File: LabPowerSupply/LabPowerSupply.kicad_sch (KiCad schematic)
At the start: 82 parts, among them SW00 7, SW01 8, SW02 7, SW03 Voltage 1, SW04 Channel 1, SW10 4, SW11 5, SW12 6, SW13 Current 1, SW14 Channel 2, SW20 1, SW21 2, SW22 3, SW23 Voltage 2, SW24 Confirm, SW30 Decimal, SW31 0, SW32 Backspace, SW33 Current 2, SW34 Cancel

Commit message: tmp
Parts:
- R1_ADC, R2_ADC: footprint (none) -> Resistor_SMD:R_1210_3225Metric
- gave numbers to parts that had none: 1
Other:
- added sheet TransformerBR (TransformerBR.kicad_sch)
- moved on the sheet: C1_Charge, C2_Charge, D1_Charge, D2_Charge, Q_Charge, R41, R42, R43, R44, R45, R46, R47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

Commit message: Fixing my screwup
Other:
- removed sheet TransformerBR
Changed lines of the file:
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@@
     )
-  )
-  (hierarchical_label "AC Power" (shape input) (at 16.51 34.29 0)
-    (effects (font (size 1.27 1.27)) (justify left))
   )
   (symbol (lib_id "power:+3V3") (at 116.84 54.61 0) (unit 1)
@@
     (pin "1")
   )
-  (sheet (at 12.7 12.7) (size 96.52 45.72) (fields_autoplaced)
-    (stroke (width 0.1524) (type solid) (color 0 0 0 0))
-    (fill (color 0 0 0 0.0000))
-    (property "Sheet name" "TransformerBR" (id 0) (at 12.7 11.9884 0)
-      (effects (font (size 1.27 1.27)) (justify left bottom))
-    )
-    (property "Sheet file" "TransformerBR.kicad_sch" (id 1) (at 12.7 59.0046 0)
-      (effects (font (size 1.27 1.27)) (justify left top))
-    )
-  )
   (sheet_instances
     (path "/" (page "1"))
-    (path "/a7d0e103-1391-4f13-b0bc-d947ebd08577" (page "2"))
   )
   (symbol_instances

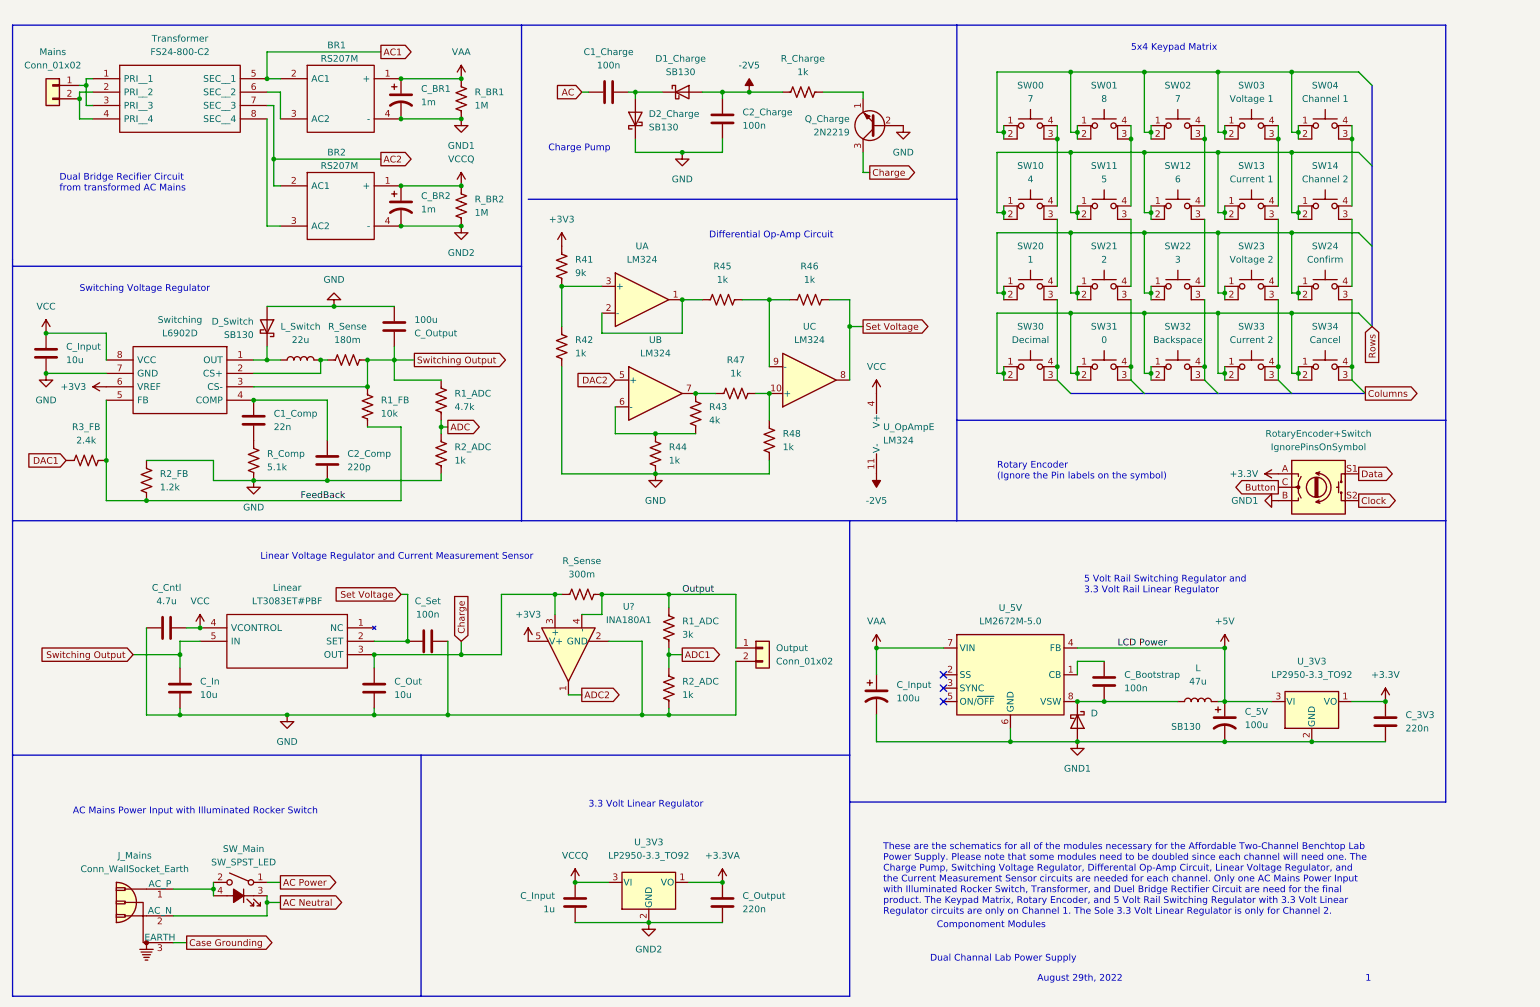
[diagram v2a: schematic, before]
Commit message: basic hierarchiral schematics
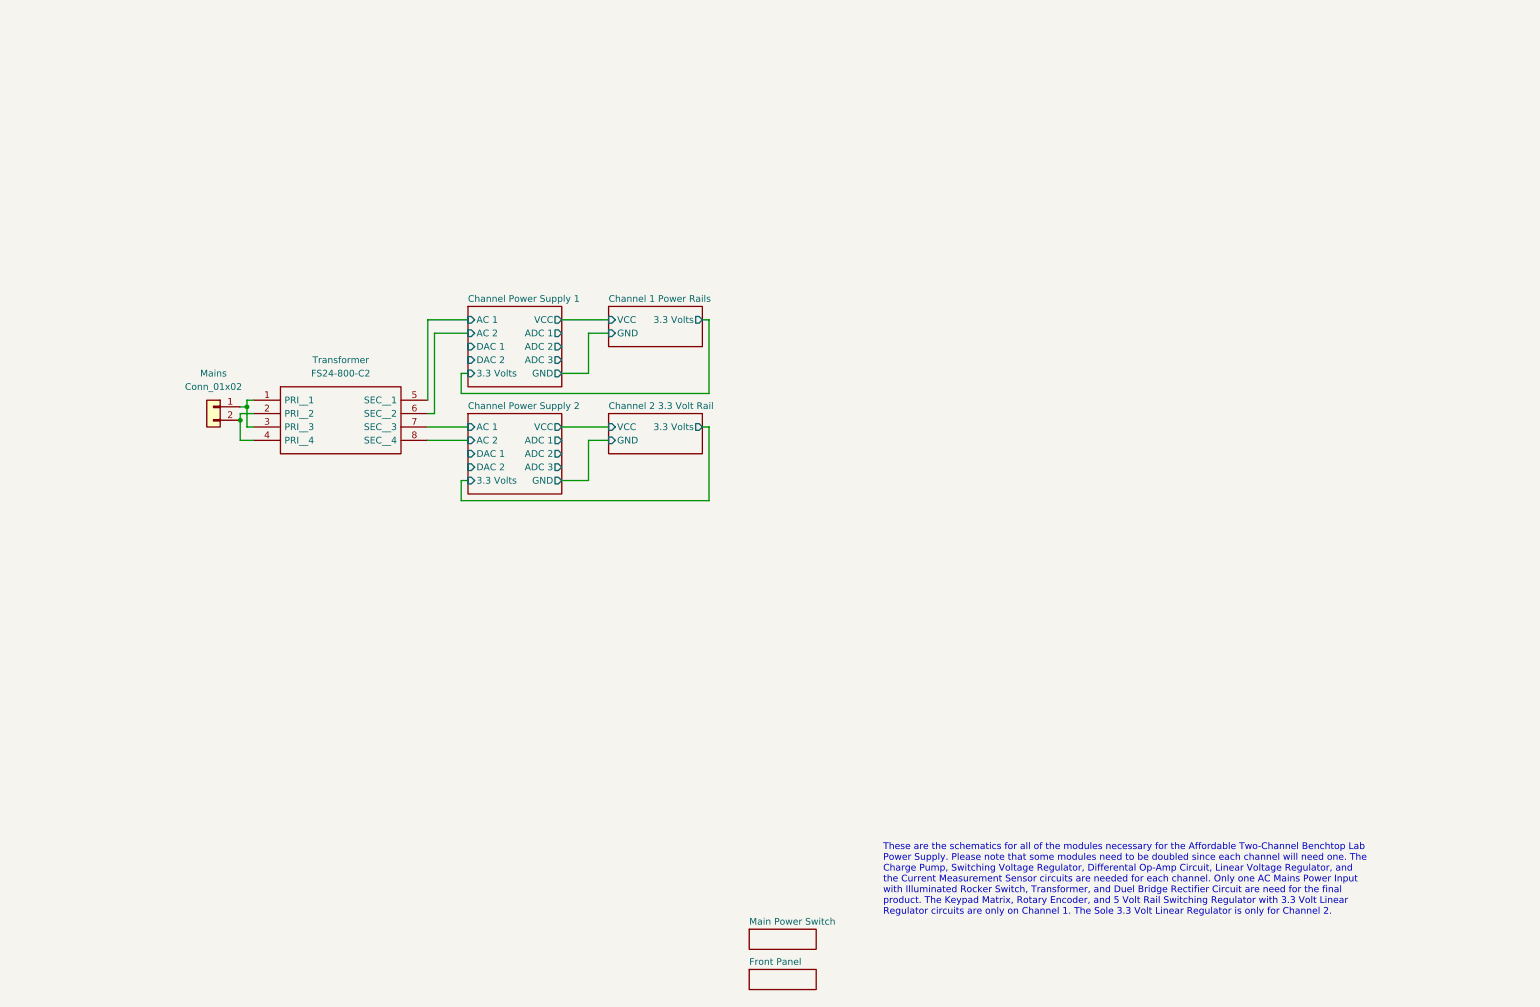
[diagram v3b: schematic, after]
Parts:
- removed BR1, BR2: RS207M, SamacSys_Parts:RS207M, symbol SamacSys_Parts:RS207M
- removed C1_Charge, C2_Charge, C_Bootstrap, C_Set: 100n, Capacitor_SMD:C_1210_3225Metric, symbol Device:C
- removed C1_Comp: 22n, Capacitor_SMD:C_1210_3225Metric, symbol Device:C
- removed C2_Comp: 220p, Capacitor_SMD:C_1210_3225Metric, symbol Device:C
- removed C_3V3, C_Output: 220n, Capacitor_SMD:C_1210_3225Metric, symbol Device:C
- removed C_5V, C_Input: 100u, Capacitor_THT:CP_Radial_D12.5mm_P5.00mm, symbol Device:C_Polarized_US
- removed C_BR1, C_BR2: 1m, Capacitor_THT:C_Radial_D12.5mm_H25.0mm_P5.00mm, symbol Device:C_Polarized_US
- removed C_Cntl: 4.7u, Capacitor_SMD:C_1210_3225Metric, symbol Device:C
- removed C_In, C_Out: 10u, Capacitor_SMD:C_1210_3225Metric, symbol Device:C
- removed C_Input: 10u, symbol Device:C
- removed C_Input: 1u, Capacitor_SMD:C_1210_3225Metric, symbol Device:C
- removed C_Output: 100u, Capacitor_SMD:C_1210_3225Metric, symbol Device:C
- removed D, D1_Charge, D2_Charge, D_Switch: SB130, Diode_THT:D_DO-41_SOD81_P10.16mm_Horizontal, symbol Diode:SB130
- removed J_Mains: Conn_WallSocket_Earth, symbol Connector:Conn_WallSocket_Earth
- removed L: 47u, Inductor_SMD:L_1210_3225Metric, symbol Device:L
- removed L_Switch: 22u, Inductor_SMD:L_1210_3225Metric, symbol Device:L
- removed Linear: LT3083ET#PBF, TO170P457X1022X2306-5P, symbol SamacSys_Parts:LT3083ET#PBF
- removed Output: Conn_01x02, Connector_Wire:SolderWire-2sqmm_1x02_P7.8mm_D2mm_OD3.9mm, symbol Connector_Generic:Conn_01x02
- removed Q_Charge: 2N2219, Package_TO_SOT_THT:TO-39-3, symbol Transistor_BJT:2N2219
- removed R1_ADC: 4.7k, Resistor_SMD:R_1210_3225Metric, symbol Device:R_US
- removed R1_ADC: 3k, Resistor_SMD:R_1210_3225Metric, symbol Device:R_US
- removed R1_FB: 10k, Resistor_SMD:R_1210_3225Metric, symbol Device:R_US
- removed R2_ADC (x2), R42, R44, R45, R46, R47, R48: 1k, Resistor_SMD:R_1210_3225Metric, symbol Device:R_US
- removed R2_FB: 1.2k, Resistor_SMD:R_1210_3225Metric, symbol Device:R_US
- removed R3_FB: 2.4k, Resistor_SMD:R_1210_3225Metric, symbol Device:R_US
- removed R41: 9k, Resistor_SMD:R_1210_3225Metric, symbol Device:R_US
- removed R43: 4k, Resistor_SMD:R_1210_3225Metric, symbol Device:R_US
- removed R_BR1, R_BR2: 1M, Resistor_SMD:R_1210_3225Metric, symbol Device:R_US
- removed R_Charge: 1k, symbol Device:R_US
- removed R_Comp: 5.1k, Resistor_SMD:R_1210_3225Metric, symbol Device:R_US
- removed R_Sense: 180m, Resistor_SMD:R_1210_3225Metric, symbol Device:R_US
- removed R_Sense: 300m, Resistor_SMD:R_1210_3225Metric, symbol Device:R_US
- removed RotaryEncoder+Switch: IgnorePinsOnSymbol, symbol Device:RotaryEncoder_Switch
- removed SW00, SW02: 7, Button_Switch_SMD:SW_MEC_5GSH9, symbol Switch:SW_MEC_5E
- removed SW01: 8, Button_Switch_SMD:SW_MEC_5GSH9, symbol Switch:SW_MEC_5E
- removed SW03: Voltage 1, Button_Switch_SMD:SW_MEC_5GSH9, symbol Switch:SW_MEC_5E
- removed SW04: Channel 1, Button_Switch_SMD:SW_MEC_5GSH9, symbol Switch:SW_MEC_5E
- removed SW10: 4, Button_Switch_SMD:SW_MEC_5GSH9, symbol Switch:SW_MEC_5E
- removed SW11: 5, Button_Switch_SMD:SW_MEC_5GSH9, symbol Switch:SW_MEC_5E
- removed SW12: 6, Button_Switch_SMD:SW_MEC_5GSH9, symbol Switch:SW_MEC_5E
- removed SW13: Current 1, Button_Switch_SMD:SW_MEC_5GSH9, symbol Switch:SW_MEC_5E
- removed SW14: Channel 2, Button_Switch_SMD:SW_MEC_5GSH9, symbol Switch:SW_MEC_5E
- removed SW20: 1, Button_Switch_SMD:SW_MEC_5GSH9, symbol Switch:SW_MEC_5E
- removed SW21: 2, Button_Switch_SMD:SW_MEC_5GSH9, symbol Switch:SW_MEC_5E
- removed SW22: 3, Button_Switch_SMD:SW_MEC_5GSH9, symbol Switch:SW_MEC_5E
- removed SW23: Voltage 2, Button_Switch_SMD:SW_MEC_5GSH9, symbol Switch:SW_MEC_5E
- removed SW24: Confirm, Button_Switch_SMD:SW_MEC_5GSH9, symbol Switch:SW_MEC_5E
- removed SW30: Decimal, Button_Switch_SMD:SW_MEC_5GSH9, symbol Switch:SW_MEC_5E
- removed SW31: 0, Button_Switch_SMD:SW_MEC_5GSH9, symbol Switch:SW_MEC_5E
- removed SW32: Backspace, Button_Switch_SMD:SW_MEC_5GSH9, symbol Switch:SW_MEC_5E
- removed SW33: Current 2, Button_Switch_SMD:SW_MEC_5GSH9, symbol Switch:SW_MEC_5E
- removed SW34: Cancel, Button_Switch_SMD:SW_MEC_5GSH9, symbol Switch:SW_MEC_5E
- removed SW_Main: SW_SPST_LED, symbol Switch:SW_SPST_LED
- removed Switching: L6902D, SOIC127P600X175-8N, symbol SamacSys_Parts:L6902D
- removed U, U_OpAmp: LM324, Package_SO:SOIC-14_3.9x8.7mm_P1.27mm, symbol Amplifier_Operational:LM324
- removed U?: INA180A1, Package_TO_SOT_SMD:SOT-23-5, symbol Amplifier_Current:INA180A1
- removed U_3V3 (x2): LP2950-3.3_TO92, Package_TO_SOT_THT:TO-92_Inline, symbol Regulator_Linear:LP2950-3.3_TO92
- removed U_5V: LM2672M-5.0, Package_SO:SOIC-8_3.9x4.9mm_P1.27mm, symbol Regulator_Switching:LM2672M-5.0
- Mains: footprint Connector_Wire:SolderWire-2sqmm_1x02_P7.8mm_D2mm_OD3.9mm -> Connector_TE-Connectivity:TE_MATE-N-LOK_1-770866-x_1x02_P4.14mm_Vertical
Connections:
- net Channel Power Supply 2/AC 2: now reaches Transformer.8 (SEC__4)
- net Channel Power Supply 1/AC 2: now reaches Transformer.6 (SEC__2)
- net AC1 renamed Channel Power Supply 1/AC 1
- net AC2 renamed Channel Power Supply 2/AC 1
- no-connect marks 3 -> 0
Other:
- added sheet Channel 1 Power Rails (Channel1PowerRails.kicad_sch)
- added sheet Channel 2 3.3 Volt Rail (Channel2_3V3VoltRail.kicad_sch)
- added sheet Channel Power Supply 1 (ChannelPowerSupply.kicad_sch)
- added sheet Channel Power Supply 2 (ChannelPowerSupply.kicad_sch)
- added sheet Front Panel (FrontPanel.kicad_sch)
- added sheet Main Power Switch (MainPowerSwitch.kicad_sch)
- note removed: "1"
- note removed: "3.3 Volt Linear Regulator"
- note removed: "5 Volt Rail Switching Regulator and 3.3 Volt Rail Linear Regulator"
- note removed: "5x4 Keypad Matrix"
- note removed: "AC Mains Power Input with Illuminated Rocker Switch"
- note removed: "August 29th, 2022"
- note removed: "Charge Pump"
- note removed: "Componoment Modules"
- note removed: "Differential Op-Amp Circuit"
- note removed: "Dual Bridge Recifier Circuit from transformed AC Mains"
- note removed: "Dual Channal Lab Power Supply"
- note removed: "Linear Voltage Regulator and Current Measurement Sensor"
- note removed: "Rotary Encoder (Ignore the Pin labels on the symbol)"
- note removed: "Switching Voltage Regulator"
- company: (none) -> George Mason University
- title: (none) -> Dual Channel Benchtop Lab Power Supply

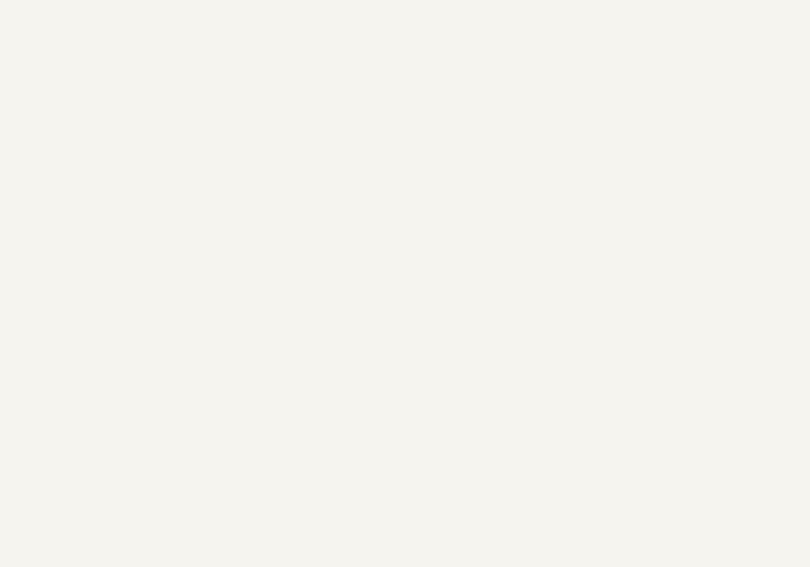
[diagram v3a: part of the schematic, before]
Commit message: Added microcontrollers to schematic
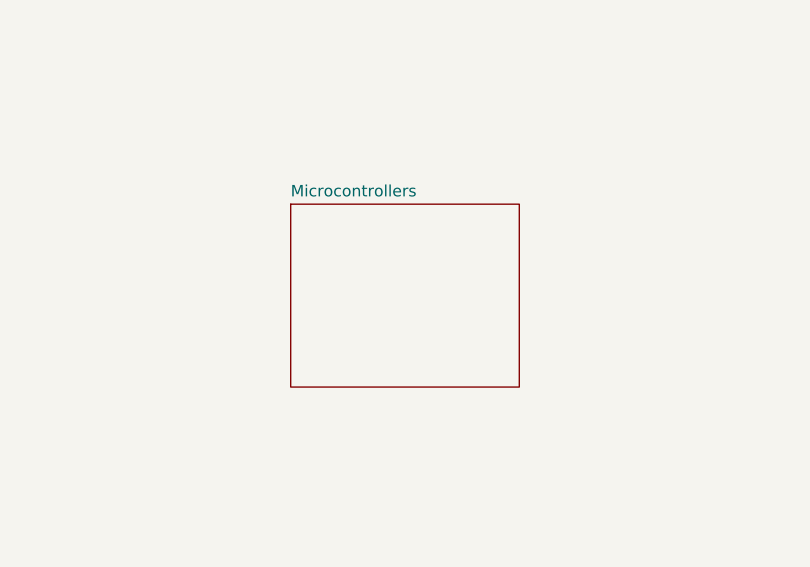
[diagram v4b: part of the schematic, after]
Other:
- added sheet Microcontrollers (Microcontrollers.kicad_sch)

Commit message: mostly finished schematic
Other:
- removed sheet Microcontrollers
- added sheet Primary Controller (PrimaryController.kicad_sch)
- added sheet Secondary Controller (SecondaryController.kicad_sch)
- sheet Channel 1 Power Rails ports: added 5 Volts; removed none
- sheet Channel Power Supply 1 ports: added ADC 4; removed none
- sheet Channel Power Supply 2 ports: added ADC 4; removed none
